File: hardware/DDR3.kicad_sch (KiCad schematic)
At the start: 1 part, among them U1 NT5CB256M16ER-FL

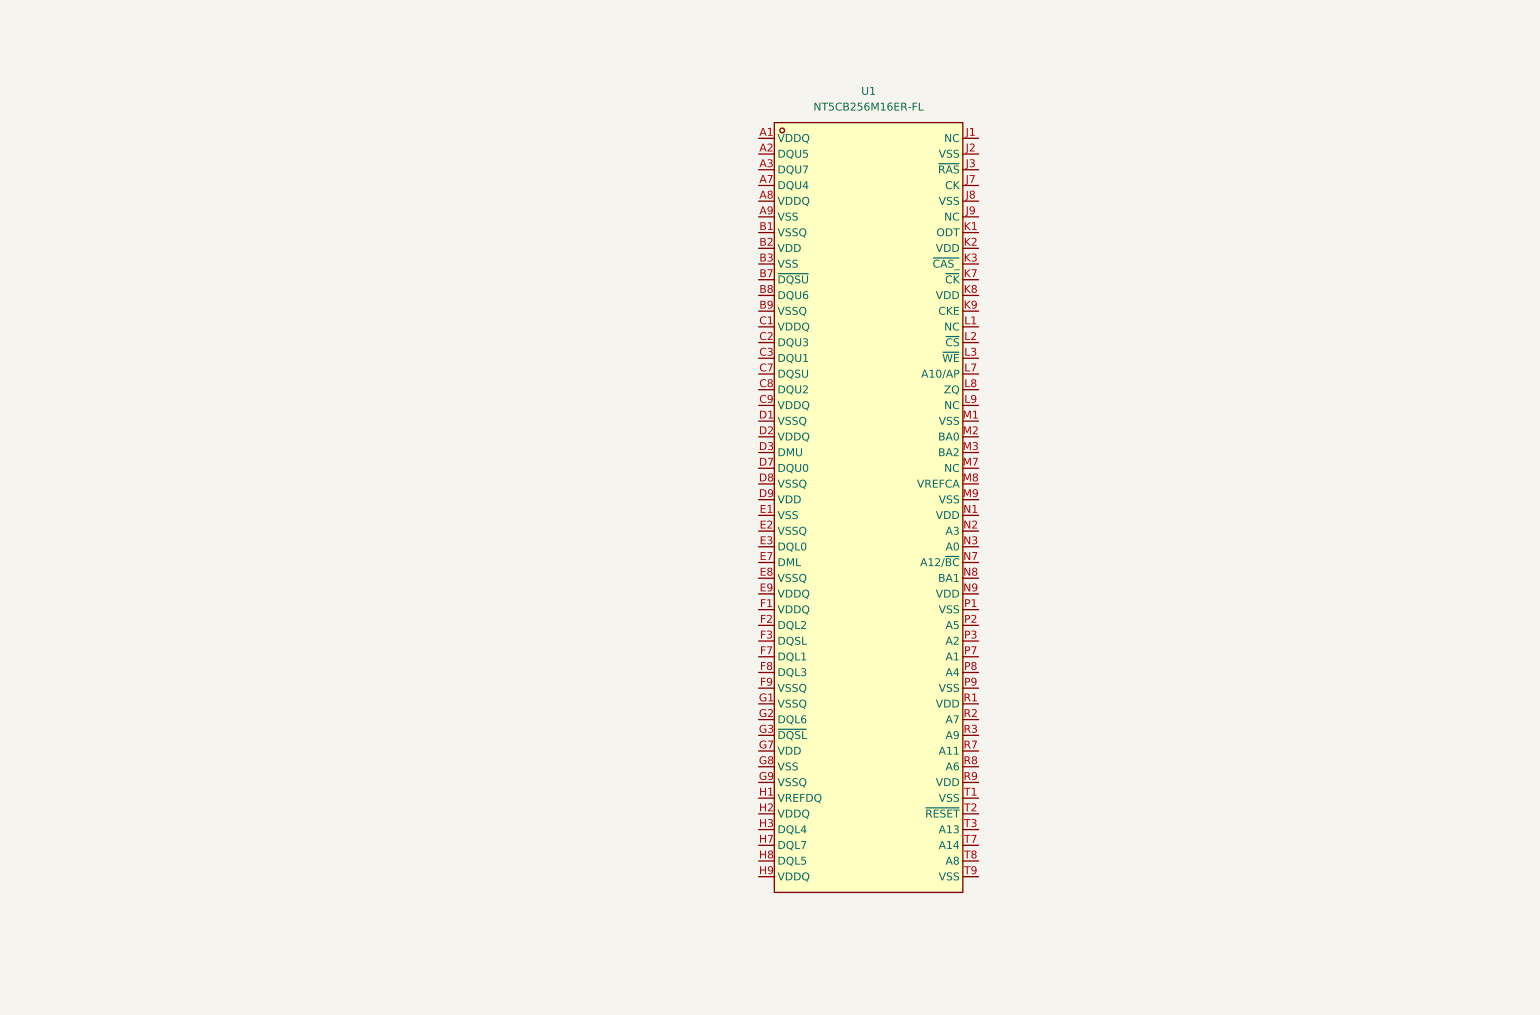
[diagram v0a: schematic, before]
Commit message: Address and Control signals of DDR3 ram routed
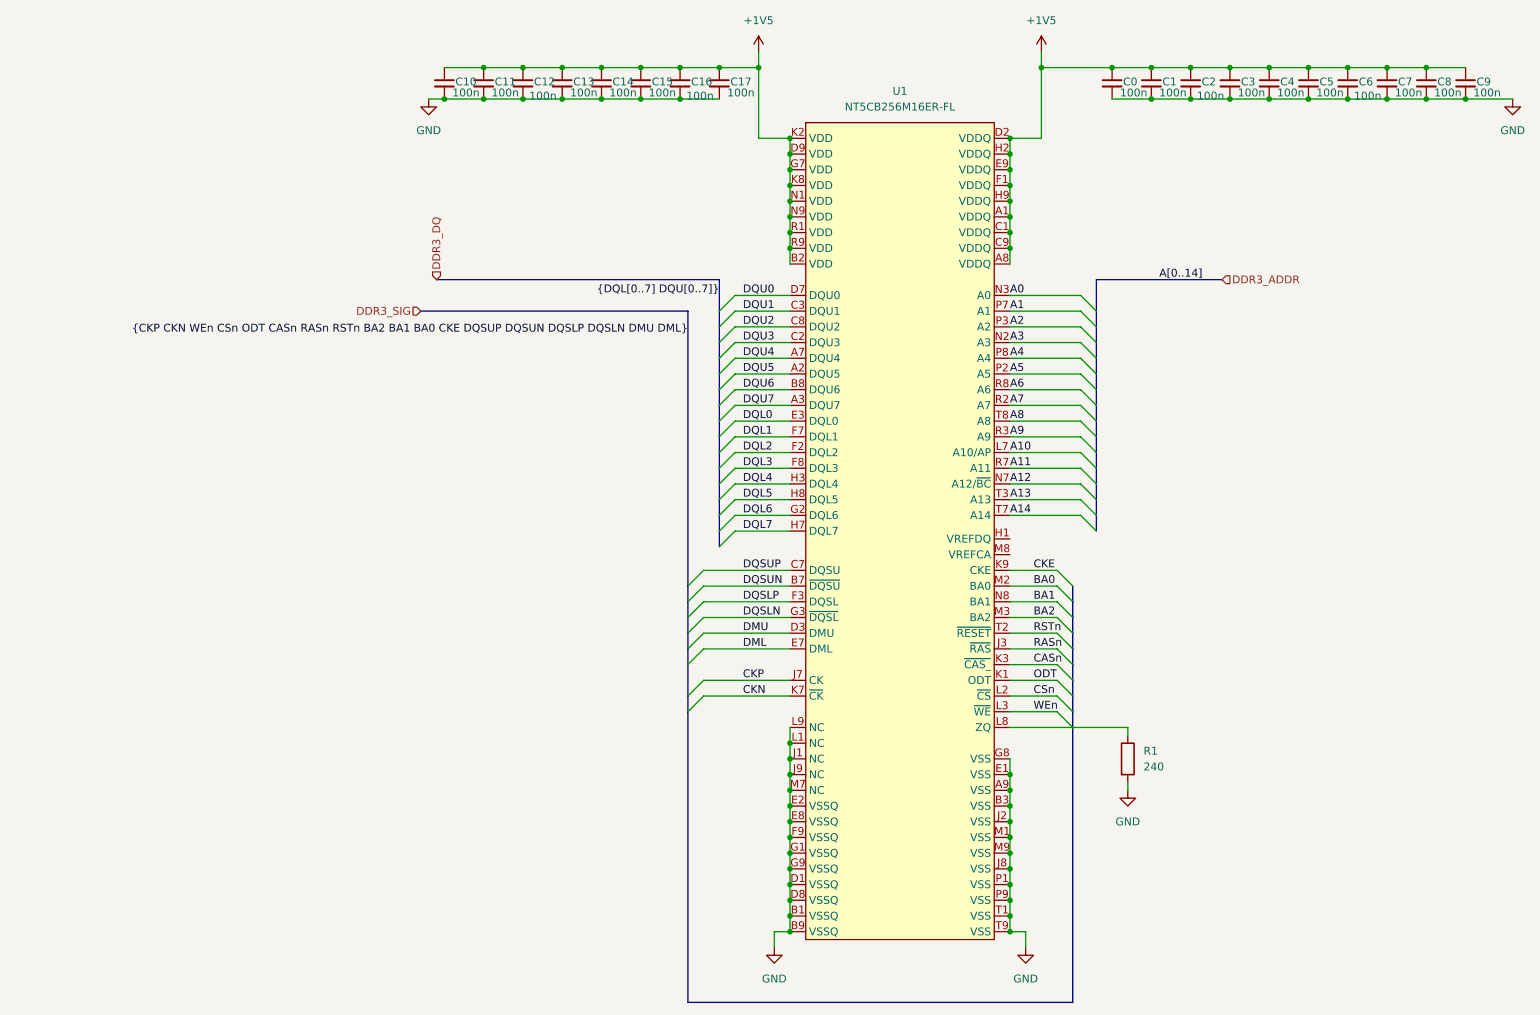
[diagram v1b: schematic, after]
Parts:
- added C0, C1, C10, C11, C12, C13, C14, C15, C16, C17, C2, C3, C4, C5, C6, C7, C8, C9: 100n, Capacitor_SMD:C_0201_0603Metric, symbol Device:C_Small
- added R1: 240, Resistor_SMD:R_0201_0603Metric, symbol Device:R
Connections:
- net +1V5: now reaches U1.A1 (VDDQ)
- net +1V5: now also U1.A8 (VDDQ), U1.B2 (VDD), U1.C1 (VDDQ), U1.C9 (VDDQ), U1.D2 (VDDQ), U1.D9 (VDD), U1.E9 (VDDQ), U1.F1 (VDDQ), U1.G7 (VDD), U1.H2 (VDDQ), U1.H9 (VDDQ), U1.K2 (VDD), U1.K8 (VDD), U1.N1 (VDD), U1.N9 (VDD), U1.R1 (VDD), U1.R9 (VDD), C0.1, C1.1, C10.1, C11.1, C12.1, C13.1, C14.1, C15.1, C16.1, C17.1, C2.1, C3.1, C4.1, C5.1, C6.1, C7.1, C8.1, C9.1
- net DQU5: now reaches U1.A2 (DQU5)
- net DQU7: now reaches U1.A3 (DQU7)
- net DQU4: now reaches U1.A7 (DQU4)
- net GND: now reaches U1.A9 (VSS)
- net GND: now also U1.B1 (VSSQ), U1.B3 (VSS), U1.B9 (VSSQ), U1.D1 (VSSQ), U1.D8 (VSSQ), U1.E1 (VSS), U1.E2 (VSSQ), U1.E8 (VSSQ), U1.F9 (VSSQ), U1.G1 (VSSQ), U1.G8 (VSS), U1.G9 (VSSQ), U1.J1 (NC), U1.J2 (VSS), U1.J8 (VSS), U1.J9 (NC), U1.L1 (NC), U1.L9 (NC), U1.M1 (VSS), U1.M7 (NC), U1.M9 (VSS), U1.P1 (VSS), U1.P9 (VSS), U1.T1 (VSS), U1.T9 (VSS), C0.2, C1.2, C10.2, C11.2, C12.2, C13.2, C14.2, C15.2, C16.2, C17.2, C2.2, C3.2, C4.2, C5.2, C6.2, C7.2, C8.2, C9.2, R1.2
- net DQSUN: now reaches U1.B7 (~{DQSU})
- net DQU6: now reaches U1.B8 (DQU6)
- net DQU3: now reaches U1.C2 (DQU3)
- net DQU1: now reaches U1.C3 (DQU1)
- net DQSUP: now reaches U1.C7 (DQSU)
- net DQU2: now reaches U1.C8 (DQU2)
- net DMU: now reaches U1.D3 (DMU)
- net DQU0: now reaches U1.D7 (DQU0)
- net DQL0: now reaches U1.E3 (DQL0)
- net DML: now reaches U1.E7 (DML)
- net DQL2: now reaches U1.F2 (DQL2)
- net DQSLP: now reaches U1.F3 (DQSL)
- net DQL1: now reaches U1.F7 (DQL1)
- net DQL3: now reaches U1.F8 (DQL3)
- net DQL6: now reaches U1.G2 (DQL6)
- net DQSLN: now reaches U1.G3 (~{DQSL})
- net DQL4: now reaches U1.H3 (DQL4)
- net DQL7: now reaches U1.H7 (DQL7)
- net DQL5: now reaches U1.H8 (DQL5)
- net RASn: now reaches U1.J3 (~{RAS})
- net CKP: now reaches U1.J7 (CK)
- net ODT: now reaches U1.K1 (ODT)
- net CASn: now reaches U1.K3 (~{CAS_})
- net CKN: now reaches U1.K7 (~{CK})
- net CKE: now reaches U1.K9 (CKE)
- net CSn: now reaches U1.L2 (~{CS})
- net WEn: now reaches U1.L3 (~{WE})
- net A10: now reaches U1.L7 (A10/AP)
- net at U1.L8 (ZQ): now also R1.1
- net BA0: now reaches U1.M2 (BA0)
- net BA2: now reaches U1.M3 (BA2)
- net A3: now reaches U1.N2 (A3)
- net A0: now reaches U1.N3 (A0)
- net A12: now reaches U1.N7 (A12/~{BC})
- net BA1: now reaches U1.N8 (BA1)
- net A5: now reaches U1.P2 (A5)
- net A2: now reaches U1.P3 (A2)
- net A1: now reaches U1.P7 (A1)
- net A4: now reaches U1.P8 (A4)
- net A7: now reaches U1.R2 (A7)
- net A9: now reaches U1.R3 (A9)
- net A11: now reaches U1.R7 (A11)
- net A6: now reaches U1.R8 (A6)
- net RSTn: now reaches U1.T2 (~{RESET})
- net A13: now reaches U1.T3 (A13)
- net A14: now reaches U1.T7 (A14)
- net A8: now reaches U1.T8 (A8)
